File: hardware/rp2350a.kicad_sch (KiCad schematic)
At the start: 48 parts, among them Q1 AP1606, Q2 AP1606, U1 TS2306A 240GF MSM 9_C2976675, U2 RP2354B_C39843328, X1 XTM25012000JT00351001

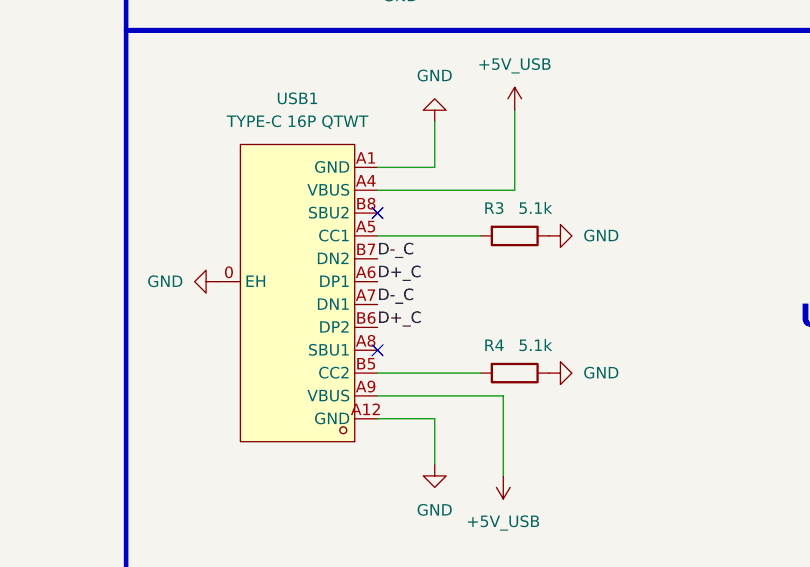
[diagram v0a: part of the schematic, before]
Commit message: Re-route with connectors
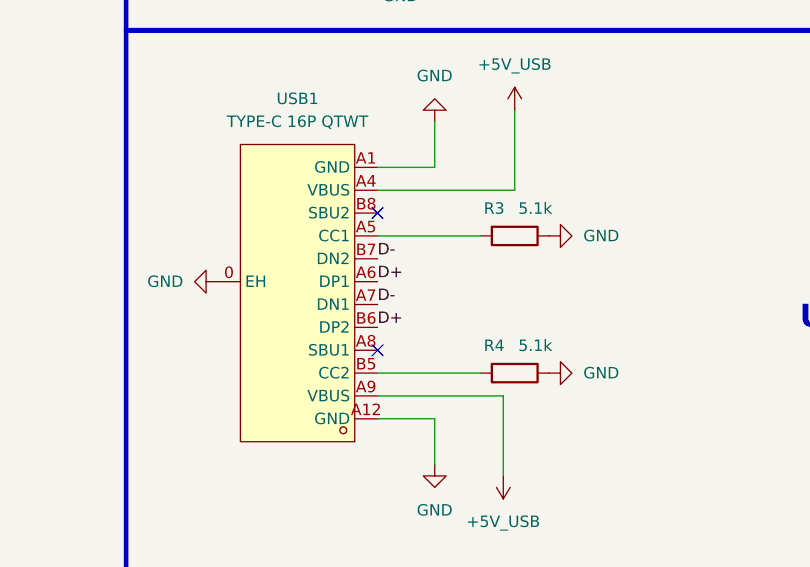
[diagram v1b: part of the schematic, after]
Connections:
- net D+_C is gone; now on net D+: USB1.A6 (DP1), USB1.B6 (DP2)
- net D-_C is gone; now on net D-: USB1.A7 (DN1), USB1.B7 (DN2)
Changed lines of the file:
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@@
-		)
-	)
-	(label "D-_C"
-		(at 88.9 275.59 0)
-		(effects
-			(font
-				(size 1.27 1.27)
-			)
-			(justify left bottom)
 		)
 	)
@@
 		)
 	)
+	(label "D-"
+		(at 88.9 275.59 0)
+		(effects
+			(font
+				(size 1.27 1.27)
+			)
+			(justify left bottom)
+		)
+	)
 	(label "ADC_VBAT"
 		(at 232.41 217.17 0)
@@
 		)
 	)
-	(label "D-_C"
+	(label "D-"
 		(at 88.9 270.51 0)
 		(effects
@@
 		)
 	)
+	(label "D+"
+		(at 88.9 273.05 0)
+		(effects
+			(font
+				(size 1.27 1.27)
+			)
+			(justify left bottom)
+		)
+	)
 	(label "D-"
 		(at 231.14 193.04 180)
@@
 		)
 	)
-	(label "D+_C"
-		(at 88.9 273.05 0)
-		(effects
-			(font
-				(size 1.27 1.27)
-			)
-			(justify left bottom)
-		)
-	)
 	(label "SPI1.MISO"
 		(at 312.42 212.09 180)
@@
 		)
 	)
-	(label "D+_C"
+	(label "D+"
 		(at 88.9 278.13 0)
 		(effects
